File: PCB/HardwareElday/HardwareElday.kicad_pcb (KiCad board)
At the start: 2 copper layers, 63 x 35 mm, 16 parts, among them J1 Conn_01x04, J3 Conn_01x03, Q1 NMOS, Q2 NMOS, Q3 NPN, Q4 PNP

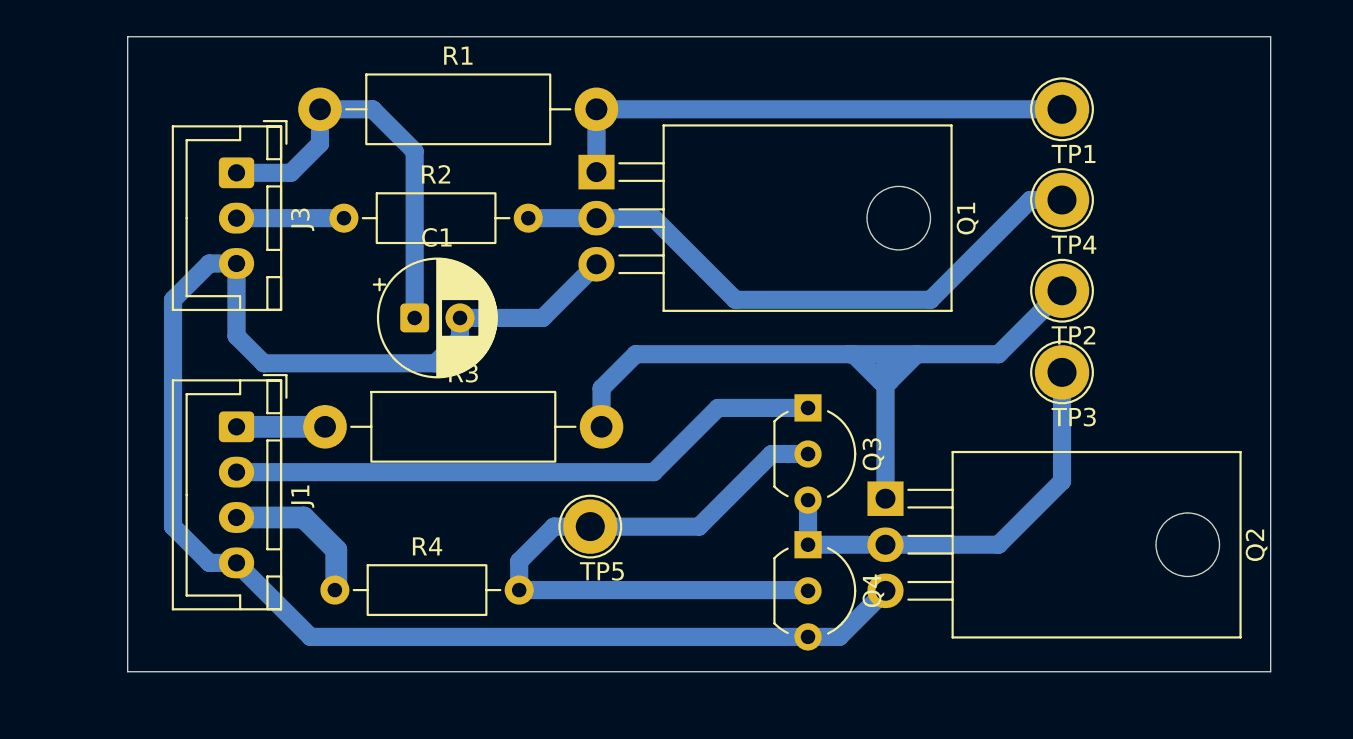
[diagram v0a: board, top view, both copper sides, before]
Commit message: Update file report and simulation
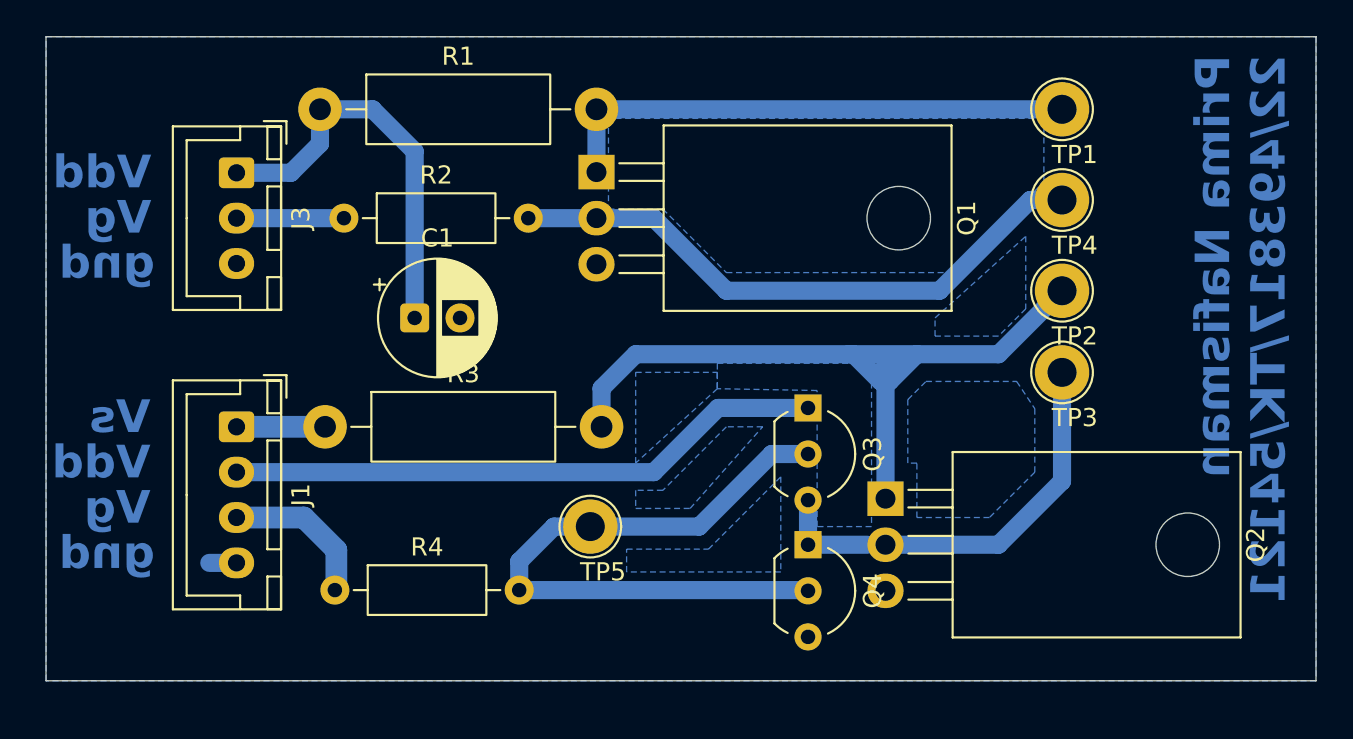
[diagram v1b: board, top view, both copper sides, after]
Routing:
- net GNDREF: track 87.1 -> 1.50 mm
- added copper zone on B.Cu, net GNDREF
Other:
- board size 63 x 35 mm -> 70 x 35.5 mm
- board text added: "Prima Nafisman 22/493817/TK/54121"
- board text added: "Vdd"
- board text added: "Vg"
- board text added: "Vs"
- board text added: "gnd"

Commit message: Update file report and simulation
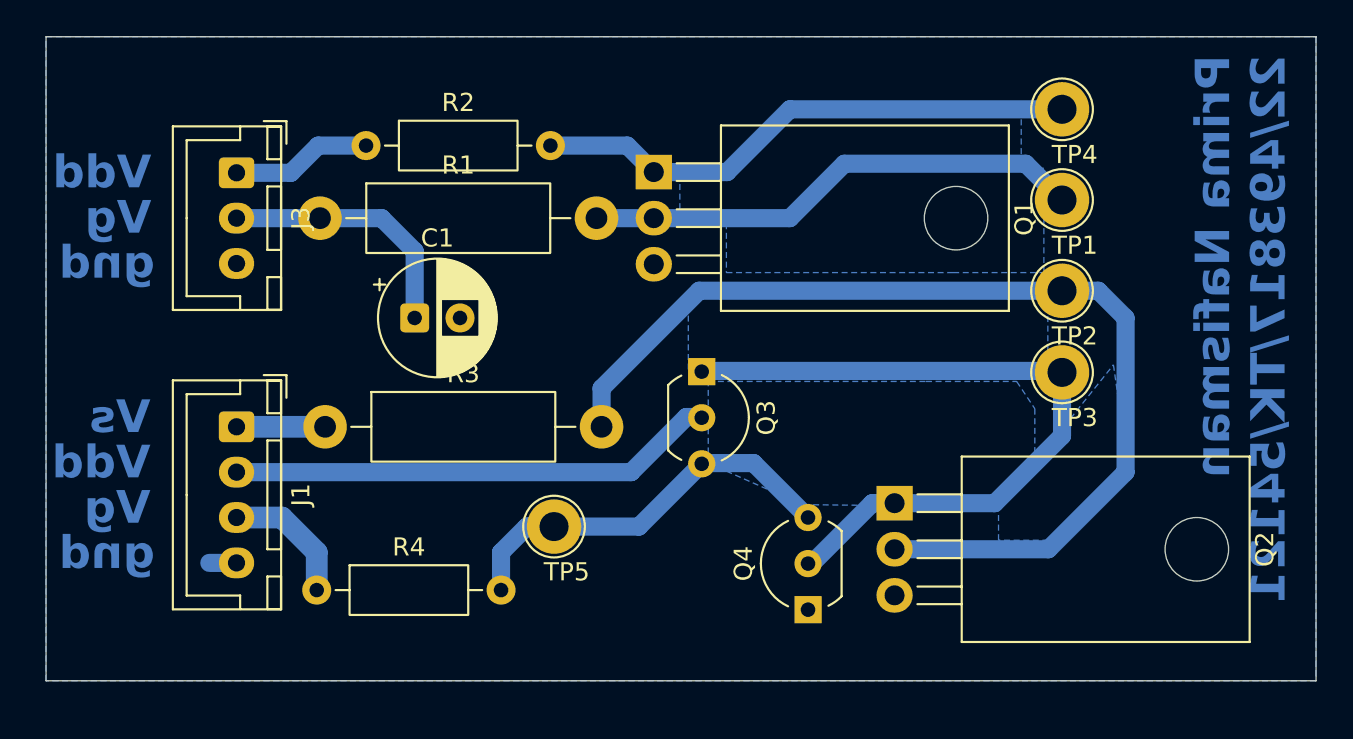
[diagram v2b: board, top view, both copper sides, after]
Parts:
- moved Q3 6.19 mm to (101.6, 115.0)
- moved R1 6.00 mm to (80.6, 106.5)
- moved TP1 5.00 mm to (121.5, 105.5)
- moved TP4 5.00 mm to (121.5, 100.5)
- moved R2 4.18 mm to (83.1, 102.5)
- moved Q4 3.58 mm to (107.5, 128.1), turned to 90 degrees
- moved Q1 3.16 mm to (99.0, 104.0)
- moved TP5 2.00 mm to (93.5, 123.5)
- moved R4 1.00 mm to (80.4, 127.0)
- moved Q2 0.56 mm to (112.3, 122.2)
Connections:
- C1 pad 1: Net-(J3-Pin_1) -> Net-(J3-Pin_2)
- J3 pad 1: Net-(J3-Pin_1) -> Vg
- J3 pad 2: Vg -> Net-(J3-Pin_2)
- Q1 pad 1: Net-(Q1-D) -> Net-(Q1-G)
- Q1 pad 2: Net-(Q1-G) -> Net-(Q1-D)
- Q2 pad 1: Net-(Q2-D) -> Net-(Q2-G)
- Q2 pad 2: Net-(Q2-G) -> Net-(Q2-D)
- Q3 pad 1: Vd -> Net-(Q2-G)
- Q3 pad 2: Net-(Q3-B) -> Vd
- Q3 pad 3: Net-(Q2-G) -> Net-(Q3-B)
- Q4 pad 1: Net-(Q2-G) -> GNDREF
- Q4 pad 2: Net-(Q3-B) -> Net-(Q2-G)
- Q4 pad 3: GNDREF -> Net-(Q3-B)
- R1 pad 1: Net-(J3-Pin_1) -> Net-(J3-Pin_2)
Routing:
- net Net-(J3-Pin_1): track 22.5 -> 0.00 mm
- net Net-(Q2-G): track 23.0 -> 40.3 mm
- net Net-(Q2-D): track 42.2 -> 56.8 mm
- net Net-(J3-Pin_2): track 0.00 -> 14.3 mm
- net Net-(Q3-B): track 35.9 -> 22.3 mm
- net Vd: track 33.0 -> 26.9 mm
- net Net-(Q1-G): track 33.1 -> 30.2 mm
- net Vg: track 5.92 -> 7.76 mm
- net Net-(Q1-D): track 29.1 -> 27.7 mm
- net Net-(J1-Pin_3): track 8.48 -> 7.30 mm
